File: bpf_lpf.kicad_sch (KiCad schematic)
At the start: 17 parts, among them K1 DPDT-12V

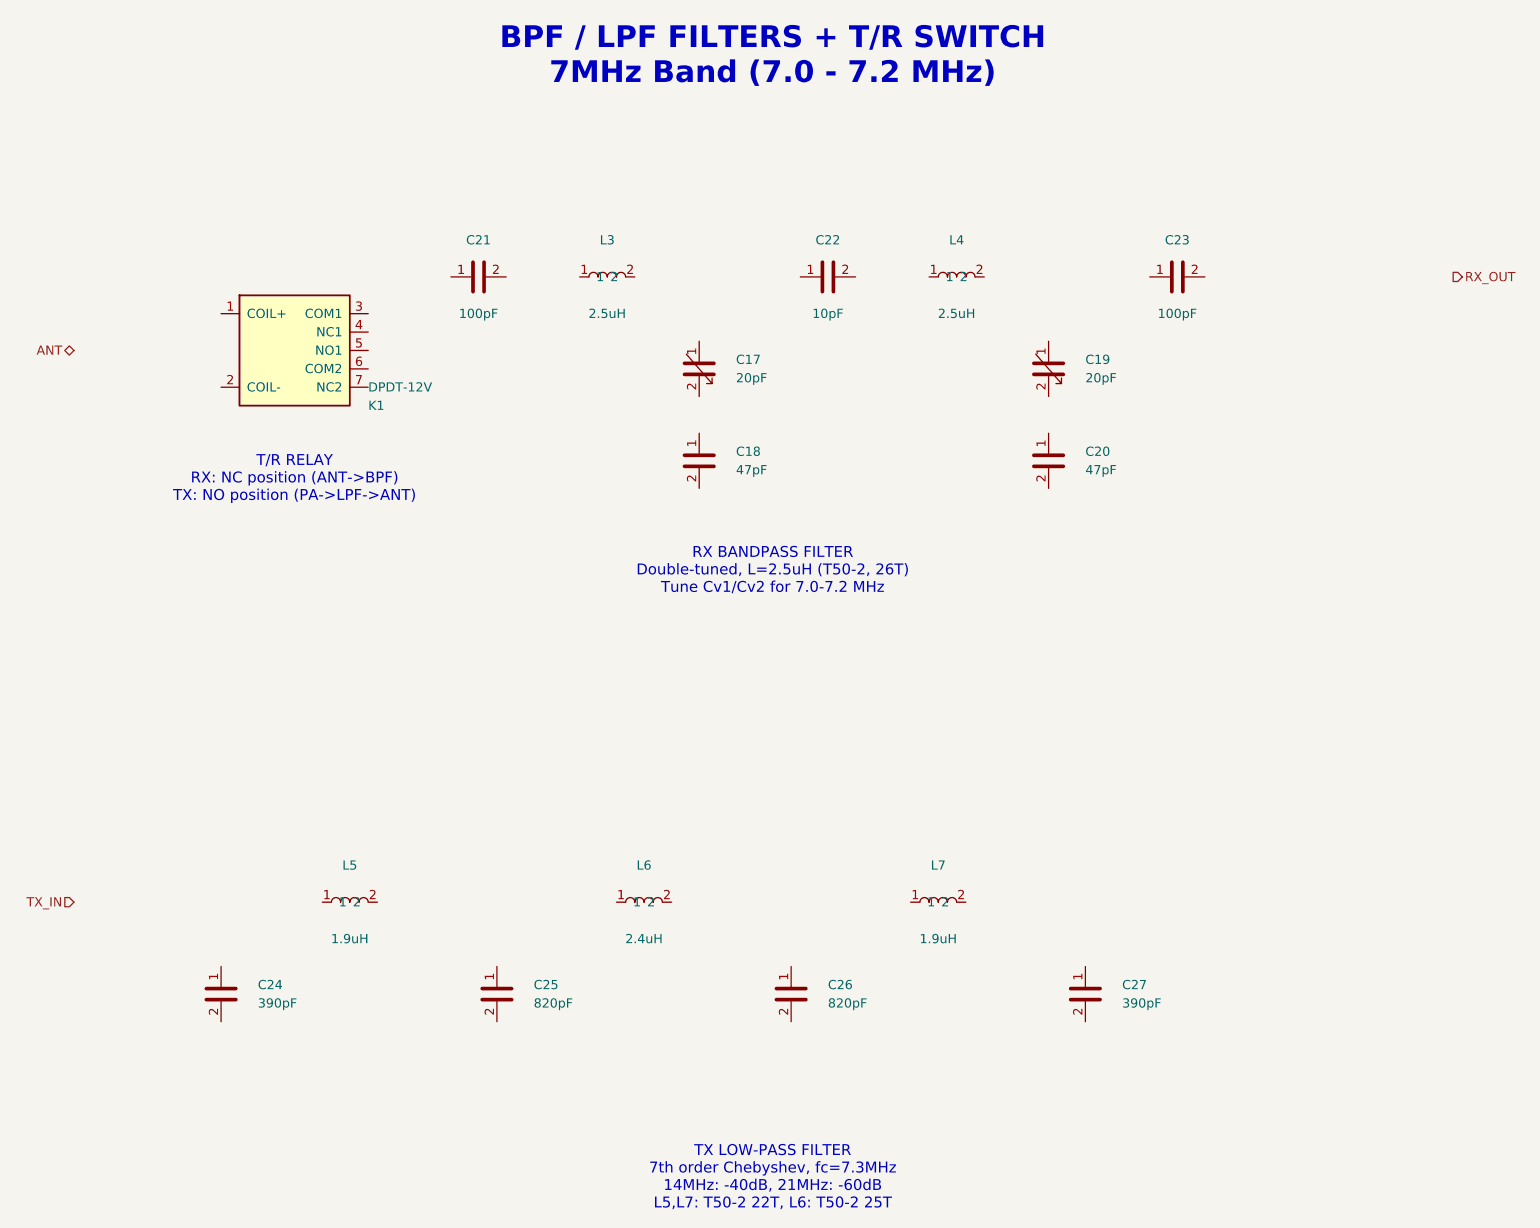
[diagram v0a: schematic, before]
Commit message: Add initial PCB layout with complete component placement
- Create 2-layer PCB (200x100mm) based on KiCad schematic import
- Place all components including Arduino Nano, Si5351, SA612 mixers, SSD1306 OLED
- Position audio amplifier (LM386), voltage regulators (7805/7808), crystal filters
- Add discrete components: resistors, capacitors, inductors, diodes, transistors
- Include connectors for power (DC jack), antenna, speaker, and microphone
- Update .gitignore to exclude fp-info-cache and backup directories
- Update schematic symbols for all circuit blocks (audio, BPF/LPF, control, IF filter, mixer/modulator, power amp, power supply)
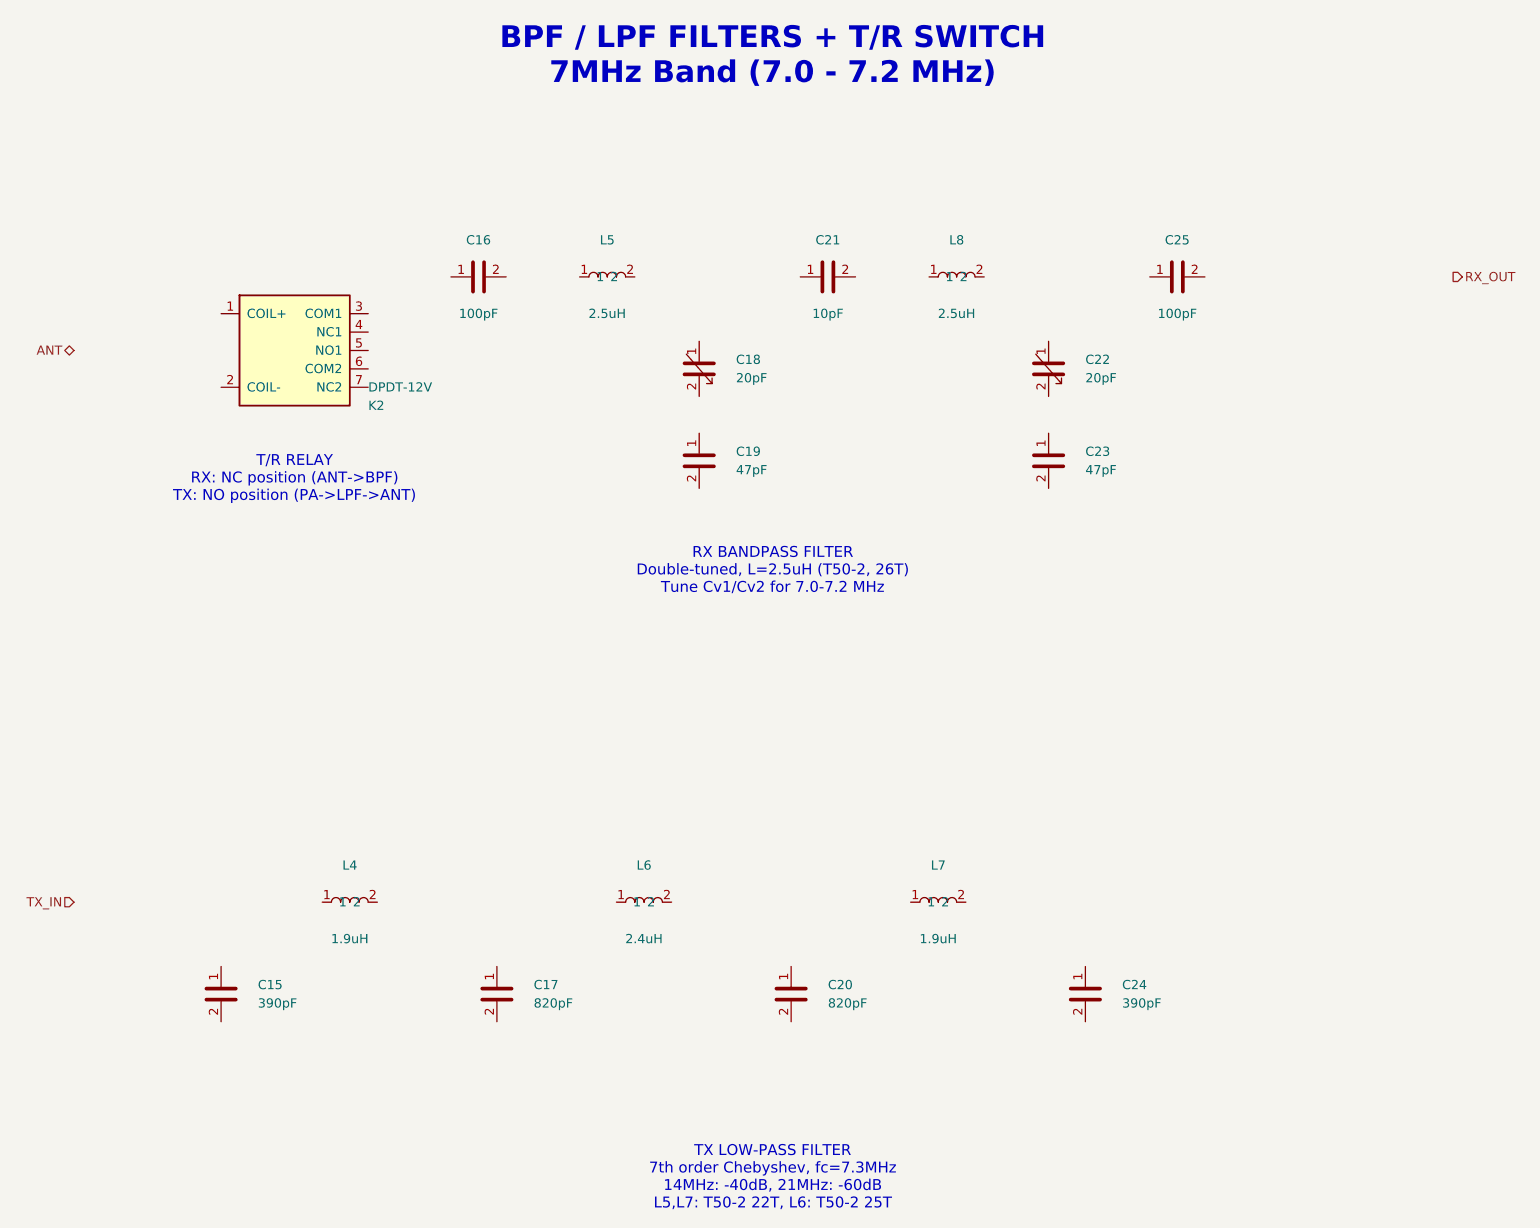
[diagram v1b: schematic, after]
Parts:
- removed C17, C19: 20pF, symbol Device:C_Variable
- removed C18: 47pF, symbol Device:C
- removed C22: 10pF, symbol Device:C
- removed C26: 820pF, symbol Device:C
- removed C27: 390pF, symbol Device:C
- removed K1: DPDT-12V, symbol Relay:DPDT_Relay
- removed L3: 2.5uH, symbol Device:L
- added C15: 390pF, Capacitor_THT:C_Disc_D5.0mm_W2.5mm_P5.00mm, symbol Device:C
- added C16: 100pF, Capacitor_THT:C_Disc_D5.0mm_W2.5mm_P5.00mm, symbol Device:C
- added C17: 820pF, Capacitor_THT:C_Disc_D5.0mm_W2.5mm_P5.00mm, symbol Device:C
- added C18, C22: 20pF, Capacitor_THT:C_Disc_D5.0mm_W2.5mm_P5.00mm, symbol Device:C_Variable
- added C19: 47pF, Capacitor_THT:C_Disc_D5.0mm_W2.5mm_P5.00mm, symbol Device:C
- added K2: DPDT-12V, Connector_PinHeader_2.54mm:PinHeader_1x07_P2.54mm_Vertical, symbol Relay:DPDT_Relay
- added L8: 2.5uH, Inductor_THT:L_Radial_D8.7mm_P5.00mm_Fastron_07HCP, symbol Device:L
- C20: value 47pF -> 820pF; footprint (none) -> Capacitor_THT:C_Disc_D5.0mm_W2.5mm_P5.00mm
- C21: value 100pF -> 10pF; footprint (none) -> Capacitor_THT:C_Disc_D5.0mm_W2.5mm_P5.00mm
- C23: value 100pF -> 47pF; footprint (none) -> Capacitor_THT:C_Disc_D5.0mm_W2.5mm_P5.00mm
- C24: footprint (none) -> Capacitor_THT:C_Disc_D5.0mm_W2.5mm_P5.00mm
- C25: value 820pF -> 100pF; footprint (none) -> Capacitor_THT:C_Disc_D5.0mm_W2.5mm_P5.00mm
- L4: value 2.5uH -> 1.9uH; footprint (none) -> Inductor_THT:L_Radial_D8.7mm_P5.00mm_Fastron_07HCP
- L5: value 1.9uH -> 2.5uH; footprint (none) -> Inductor_THT:L_Radial_D8.7mm_P5.00mm_Fastron_07HCP
- L6, L7: footprint (none) -> Inductor_THT:L_Radial_D8.7mm_P5.00mm_Fastron_07HCP
